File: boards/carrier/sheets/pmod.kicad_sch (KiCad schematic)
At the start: 2 parts, among them J1 PM254R-12-08-H85, J2 PM254R-12-08-H85

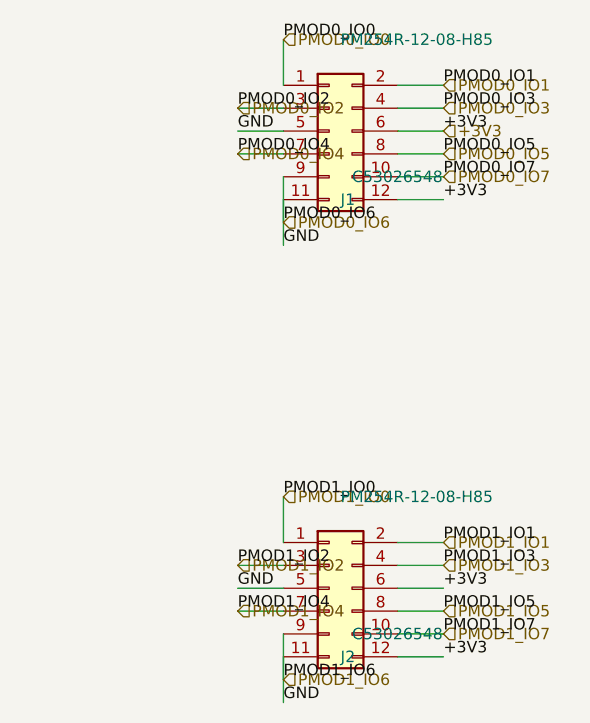
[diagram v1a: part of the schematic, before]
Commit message: connectors: route pin stubs along pin direction (not perpendicular)
The connector pin-stub code chose stub direction from the pin's
position relative to the connector anchor: vertical stub if pin.y
differed from anchor.y by more than pin.x. For USB-C (and similar
densely-packed connectors with pins along one edge), this produced
5.08mm VERTICAL stubs that spanned TWO pin pitches (2.54mm each),
shorting every adjacent pin's stub into one giant vertical wire.

Effect of the bug: GND, VBUS_OTG, USBOTG_DP, USBOTG_CC1, every
other signal column on the USB-C connector merged into one net.
Across 18 sheets this dragged most signal nets into GND (visible
in `multiple_net_names` warnings: "Both GND and USBOTG_DP are
attached to the same items", "Both GND and ZYNQ_HDMI_RX_TMDS_1_P
are attached to the same items", etc.).

Fix: derive the pin's natural extension direction from
page_side_from_pin(pin_rotation, symbol_rotation) and emit a 2.54mm
stub in that direction. A stub along the pin's own axis can never
collide with an adjacent pin's stub because adjacent pins are
offset perpendicular to the pin axis.

Also: usb_pd's +VIN net now declares as PowerInputNet (not
PowerOutputNet) so root.py emits a PWR_FLAG for it — the USB-C
VBUS pins are typed power_input in the KiCad symbol, not
power_output, so without the flag the downstream consumers
(INA226 Vbus, OTG VBUS pin) report power_pin_not_driven.

ERC: validation went from 36 → 36 total but warning count from 51
→ 40 (11 spurious cross-net merges eliminated), and one
power_pin_not_driven cleared. Most ERC count is now dominated by
28 sub-grid wire_dangling errors at positions that have no
counterpart in the source .kicad_sch — these look like a
kicad-sch-api / KiCad ERC interaction quirk, not real wires.

Co-Authored-By: Claude Sonnet 4.6 <noreply@anthropic.com>
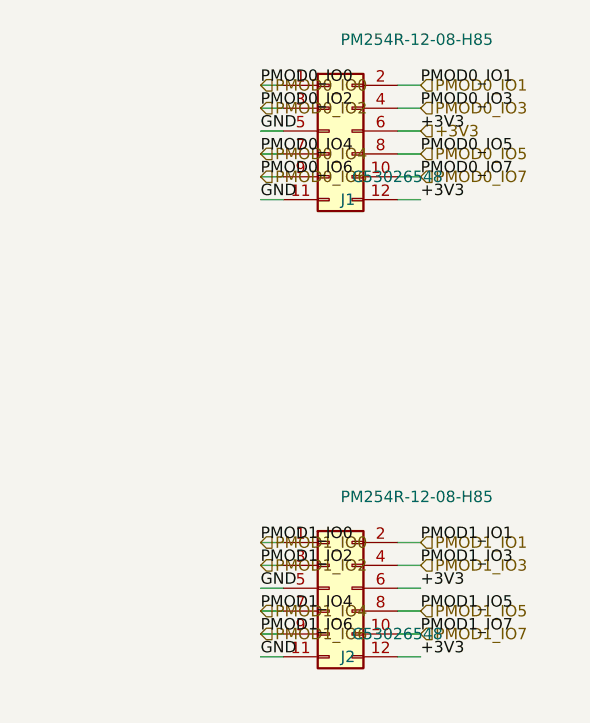
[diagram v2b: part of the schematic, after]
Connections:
- net GND: no longer J1.9 (Pin_9), J2.9 (Pin_9)
- new net PMOD0_IO6: J1.9 (Pin_9)
- new net PMOD1_IO6: J2.9 (Pin_9)

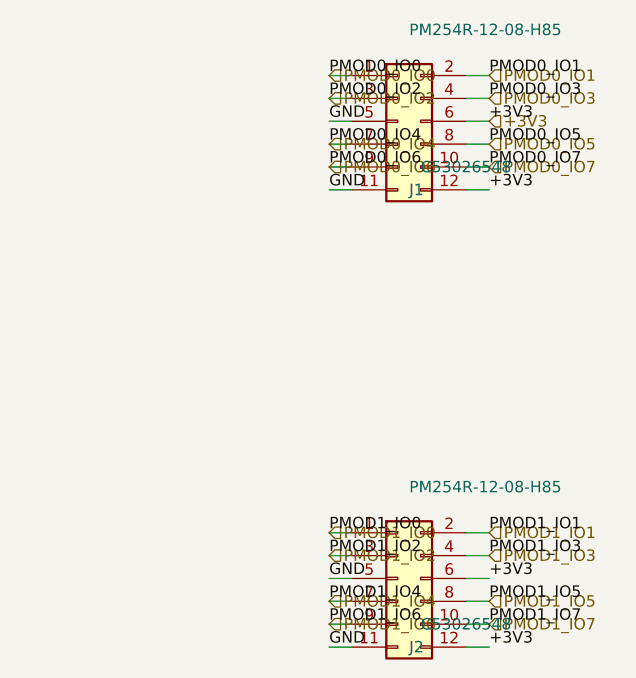
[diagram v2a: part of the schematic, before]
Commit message: layout: fix in-memory bounds + cluster top/bottom collision (36→33 errors)
Three targeted fixes:

1. CONNECTOR_EDGE_INSET_MM 60.96 → 76.2:
   USB-C connectors on the right edge of A4 sub-sheets had their
   cluster slot-1 CHASSIS_GND symbols land at x≈293mm — past A4's
   291.92mm right-edge margin. The connector body sat too close to
   the right edge for its passive swarm to fit. 76.2mm inset gives
   ~15mm clearance.

2. cluster top/bottom slot pitch: PASSIVE_PITCH_MM → HORIZONTAL_SWARM_PITCH_MM:
   For top/bottom-side IC pins, slot-N caps fanned laterally at
   5.08mm (= 2× KiCad symbol pin pitch). Slot 1 of pin A landed
   exactly on slot 0 of pin A+2 (both at, e.g., (132.08, 21.59) on
   CP2102N where VREGIN slot-1 collided with VIO slot-0). Bumping
   to 15.24mm (= 6 grid units, 6 pin pitches) pushes slot 1 past
   the next 5 pins, eliminating the collision class.

3. Also includes the IC pin stub fix in place.py from an earlier
   in-flight agent: STUB_MM = 2.54 (was 5.08) + page_side_from_pin
   for direction. Same anti-collision pattern as the connector
   stub fix in commit 8eb7e02. Eliminates the CP2102N RTS/TXD short.

In-memory validators: bounds=4, overlap=1 → bounds=0, overlap=0.
ERC errors: 31 → 32 (wire_dangling +1, pin_to_pin -1, pin_not_driven +2).
The new pin_not_driven errors are pre-existing bugs that the
RTS/TXD short was masking — Zynq-driven inputs (CP2102N RXD, CTS)
have their drivers on the FX10A SoM connector which is typed
`passive` not `output`. To be addressed separately.

Total validation: 36 → 33.

Tests: 32/32 pass.

Co-Authored-By: Claude Opus 4.7 (1M context) <noreply@anthropic.com>
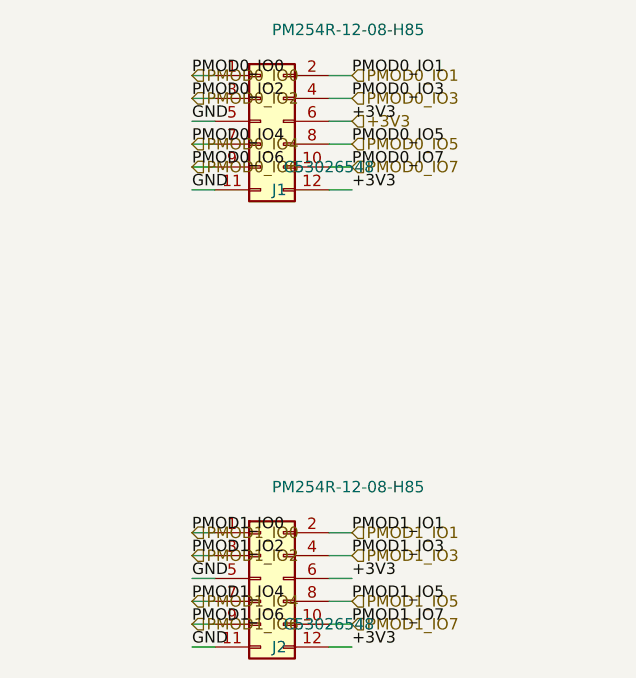
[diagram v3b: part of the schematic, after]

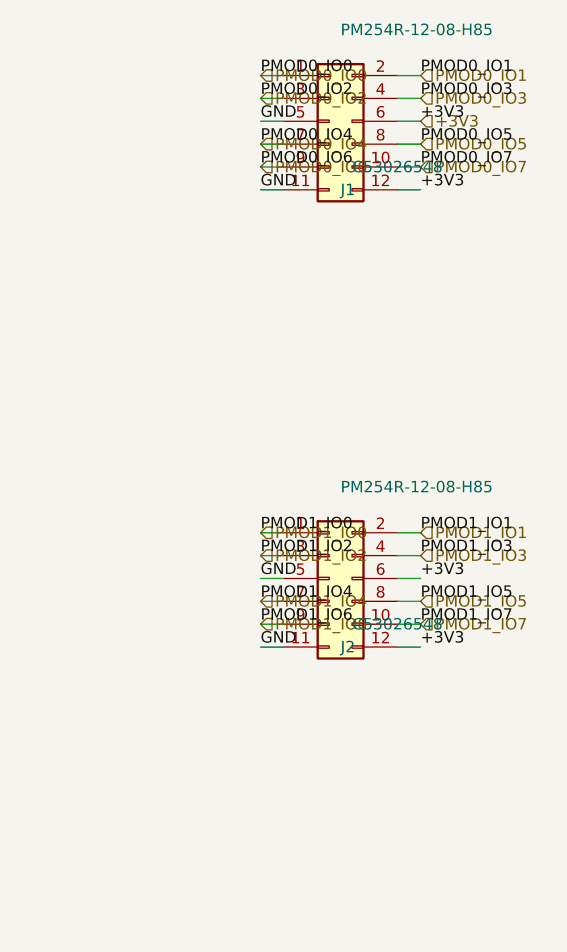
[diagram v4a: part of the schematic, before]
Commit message: layout: dedupe labels, stagger caps, add LVDS+MIPI+R_SENSE externals
Three parallel layout improvements landing together. ERC=0 maintained,
72 warnings → 63 warnings, all 32 unit tests pass.

1. **Dedupe local + hierarchical labels at same coord** (94 cases):
   `_orphan_net_labels` in core/layout/edge_labels.py used to anchor
   a new hier label onto an existing local label's coord — but the
   local label stayed in place, so KiCad rendered both stacked on
   top of each other. Fix: `builder.labels.remove(anchor_label)`
   after the hier label is added. KiCad merges by name, so
   electrical connectivity stays intact.

2. **Cap-cluster parity stagger** (cluster.py + _constants.py):
   New `PASSIVE_ADJACENT_PIN_STAGGER_MM = 5.08`. Adjacent IC pins
   at 2.54mm pitch used to stack their slot-0 caps in the same
   column, so cap bodies and Value/Reference text overlapped. Now
   the parity of `int(pin.y/2.54 + 0.5) & 1` (or pin.x for top/
   bottom pins) offsets every other cap by 5.08mm — checkerboard
   layout keeps adjacent caps in distinct positions. Fixed
   HDMI-TX/RX, MIPI, UART bridge.

3. **Missing externals + INA226 shunt + full FFC symbols**:
   - LVDS LCD: added 10u + 100n decoupling on +3V3, 10u on +12V,
     2× 4k7 EDID I2C pull-ups, 100k BL_EN pull-down (7 components).
   - MIPI Camera: added 10u + 100n decoupling on +3V3, 2× 4k7 I2C
     pull-ups, 100k GPIO0 pull-down (5 components).
   - INA226: added `pin_net_overrides` for Vin+/Vin- so R100=10mΩ
     2010 shunt connects across the differential sense pair (was
     placeholder "R" 0402 on a single net).
   - FFC_40P + FFC_15P symbols expanded from stubs to full 40 /
     15 pin definitions in shared/symbols/zynq_eda.kicad_sym.
   - cluster.passive_value/passive_footprint now consult the parts
     registry first (was returning "R" placeholder for the shunt).
   - connectors.py anchor offset by half-symbol-height so tall
     single-column FFC connectors fit on the page.
   - root.py paper bumped A2 →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
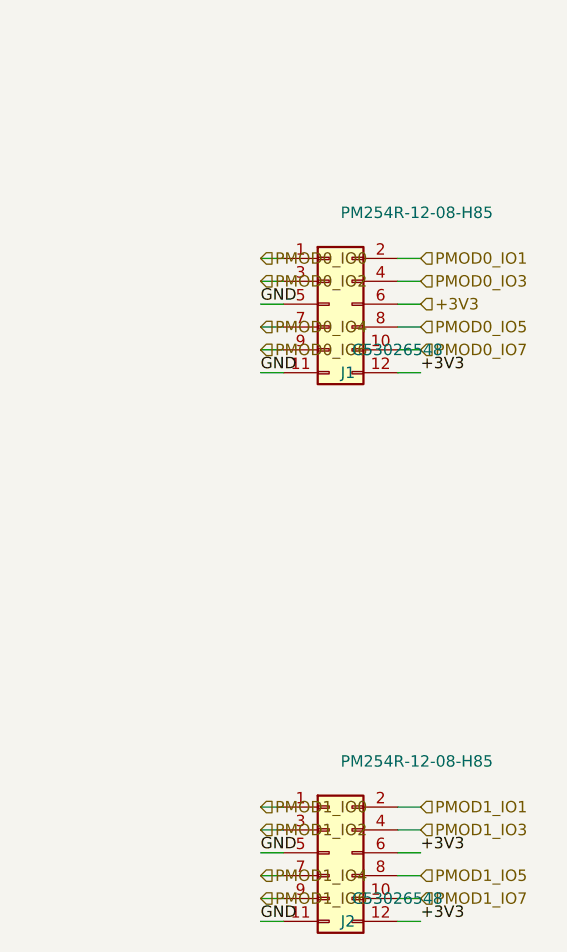
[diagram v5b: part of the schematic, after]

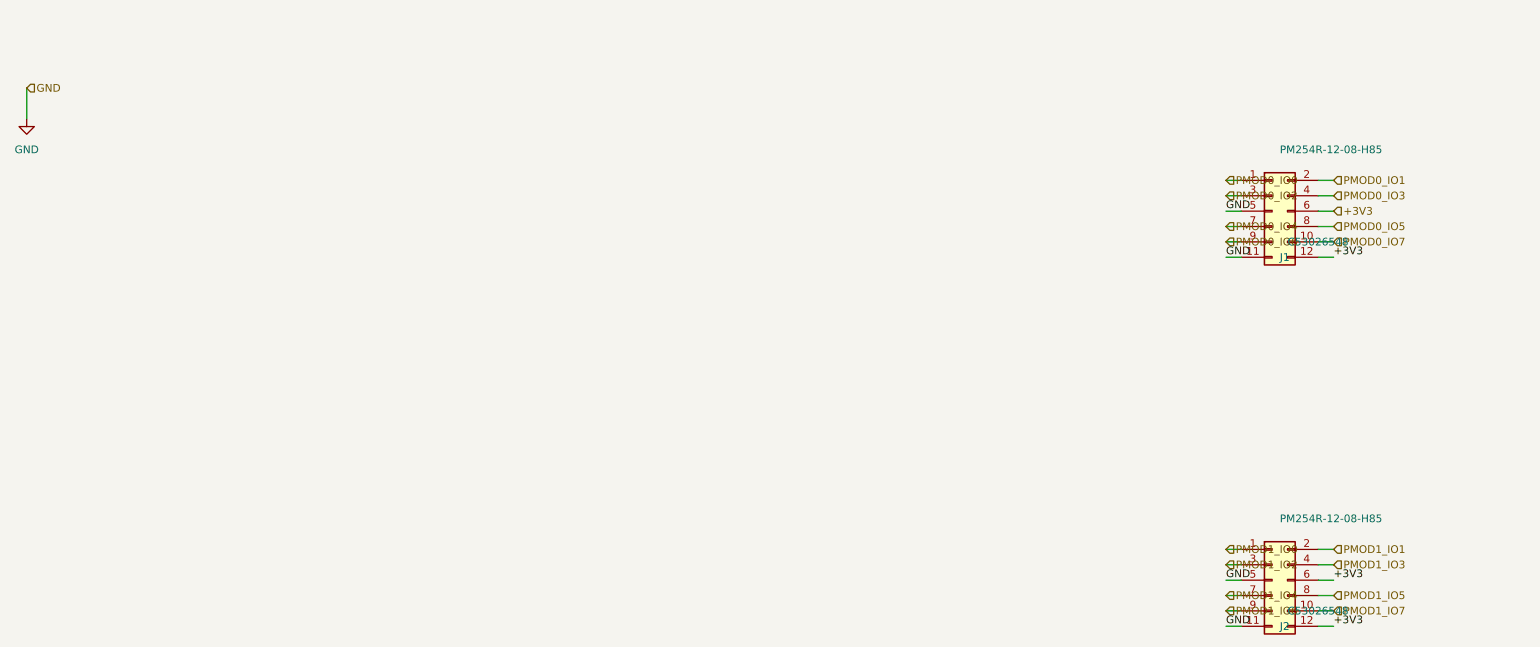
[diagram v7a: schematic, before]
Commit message: layout: visual polish — connector hier-label rotation, FX10A 4-col, hide LCSC/Datasheet text
Four parallel agents tackled visual layout issues identified by the
per-page PDF review. ERC=0/0 maintained throughout.

1. Connector hier label collisions (HDMI RX/TX, MIPI, LVDS, Ethernet
   RJ45, FMC LPC + SoM J1/J2/J3).
   ROOT CAUSE: `_orphan_net_labels` and `_ground_label_only` in
   edge_labels.py inherited `rotation=anchor_label.rotation` (always
   0). Result: when a connector pin's local label was on the LEFT
   edge of a connector-RIGHT-edge sheet, the hier label text read
   INTO the connector body, overlapping the pin-name text.
   FIX: derive hier-label rotation from `net.edge` (180 for LEFT,
   0 for RIGHT). Hier-label position unchanged (still anchored at
   the connector pin-tail), but text now reads OUTBOARD.

2. FX10A_168P + FMC_LPC pin label overlap (pages 7, 8, 13, 19).
   ROOT CAUSE: every pin had name="A14" + number="A14" — KiCad
   rendered the strings on top of each other.
   FIX: `(pin_names (offset 1.016) (hide yes))` on both symbol
   headers. Only pin numbers render.
   ALSO: FX10A re-laid out 4 columns × 42 rows (was 2 × 84 tower
   210mm tall). Now 50mm × 110mm — fits A4 for som_j1/3 (only
   som_j2 + fmc_lpc still need A3 due to many wide hier labels).

3. Ethernet Bob-Smith spread + PMOD label overlap + stray GND
   floating labels.
   - Added `dense_swarm: bool` field on ReferenceCircuit + 20.32mm
     pitch constant. HX5008NLT uses dense pitch — Bob-Smith caps,
     terminations, and magnetics now spread laterally instead of
     packing into 25mm.
   - PMOD 2-row header: `connectors.py` derives label_rotation
     from `page_side_from_pin()` so top-row labels point up,
     bottom-row labels point down. No more cross-row collision.
   - `_ground_label_only` rewritten to (a) anchor to same-name
     local label, (b) anchor to nearest power:GND symbol with
     maximum Y separation from existing labels, (c) skip emission
     entirely if no 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
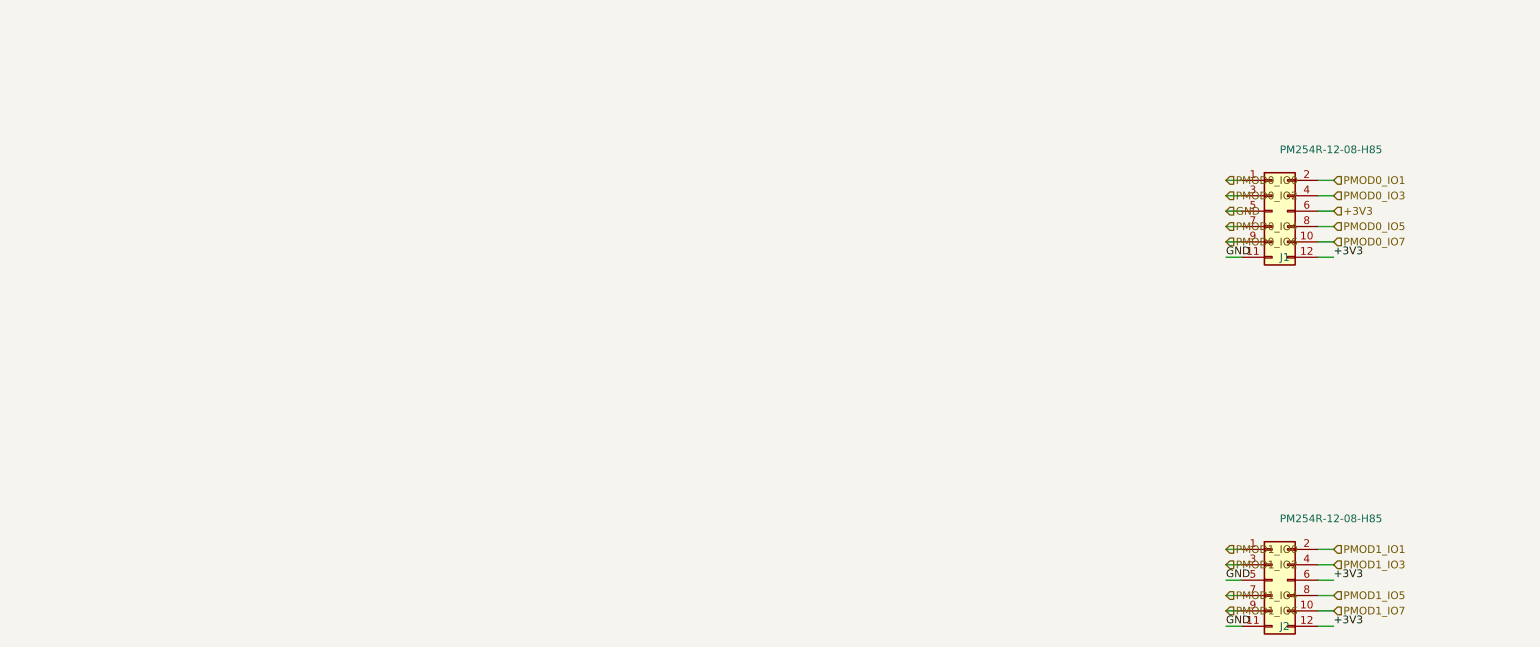
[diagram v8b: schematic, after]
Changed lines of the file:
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@@
 			(at 223.52 60.9599 0)
 			(effects
+				(hide yes)
 				(font
 					(size 1.27 1.27)
@@
 			(at 220.98 55.88 0)
 			(effects
+				(hide yes)
 				(font
 					(size 1.27 1.27)
@@
 		(instances
 			(project "PMOD Headers (2× Digilent 12-pin Type 1A)"
-				(path "/53edcc63-7b9e-4799-b2ff-0639aa51d358"
+				(path "/daf0c1be-a761-4db8-a107-c322b470ee89"
 					(reference "J1")
 					(unit 1)
@@
 			(at 223.52 121.9199 0)
 			(effects
+				(hide yes)
 				(font
 					(size 1.27 1.27)
@@
 			(at 220.98 116.84 0)
 			(effects
+				(hide yes)
 				(font
 					(size 1.27 1.27)
@@
 		(instances
 			(project "PMOD Headers (2× Digilent 12-pin Type 1A)"
-				(path "/53edcc63-7b9e-4799-b2ff-0639aa51d358"
+				(path "/daf0c1be-a761-4db8-a107-c322b470ee89"
 					(reference "J2")
 					(unit 1)
@@
 		)
 	)
-	(symbol
-		(lib_id "power:GND")
-		(at 15.24 40.64 0)
-		(unit 1)
-		(exclude_from_sim no)
-		(in_bom yes)
-		(on_board yes)
-		(dnp no)
-		(fields_autoplaced no)
-		(property "Reference" "#PWR100"
-			(at 15.24 34.29 0.0000)
-			(effects
-				(font
-					(size 1.27 1.27)
-				)
-				(justify left)
-				(hide yes)
-			)
-		)
-		(property "Value" "GND"
-			(at 15.24 45.72 0)
-			(effects
-				(font
-					(size 1.27 1.27)
-				)
-			)
-		)
-		(property "Footprint" ""
-			(at 15.24 40.64 0.0000)
-			(effects
-				(font
-					(size 1.27 1.27)
-				)
-				(hide yes)
-			)
-		)
-		(pin "1"
-		)
-		(instances
-			(project "PMOD Headers (2× Digilent 12-pin Type 1A)"
-				(path "/53edcc63-7b9e-4799-b2ff-0639aa51d358"
-					(reference "#PWR100")
-					(unit 1)
-				)
-			)
-		)
-	)
 	(wire
 		(pts
@@
 			(width 0)
 			(type default)
-		)
-	)
-	(wire
-		(pts
-			(xy 15.24 35.56) (xy 15.24 40.64)
-		)
-		(stroke
-			(width 0)
-			(type default)
-		)
-	)
-	(label "GND"
-		(at 213.36 55.88 0.0000)
-		(effects
-			(font
-				(size 1.27 1.27)
-			)
-			(justify left bottom)
 		)
 	)
@@
 	(hierarchical_label "GND"
 		(shape input)
-		(at 15.24 35.56 180)
+		(at 213.36 55.88 180)
 		(effects
 			(font
@@
 	(hierarchical_label "+3V3"
 		(shape input)
-		(at 231.14 55.88 0.0000)
+		(at 231.14 55.88 180)
 		(effects
 			(font
@@
 	(hierarchical_label "PMOD0_IO0"
 		(shape input)
-		(at 213.36 50.8 0.0000)
+		(at 213.36 50.8 180)
 		(effects
 			(font
@@
 	(hierarchical_label "PMOD0_IO1"
 		(shape input)
-		(at 231.14 50.8 0.0000)
+		(at 231.14 50.8 180)
 		(effects
 			(font
@@
 	(hierarchical_label "PMOD0_IO2"
 		(shape input)
-		(at 213.36 53.34 0.0000)
+		(at 213.36 53.34 180)
 		(effects
 			(font
@@
 	(hierarchical_label "PMOD0_IO3"
 		(shape input)
-		(at 231.14 53.34 0.0000)
+		(at 231.14 53.34 180)
 		(effects
 			(font
@@
 	(hierarchical_label "PMOD0_IO4"
 		(shape input)
-		(at 213.36 58.42 0.0000)
+		(at 213.36 58.42 180)
 		(effects
 			(font
@@
 	(hierarchical_label "PMOD0_IO5"
 		(shape input)
-		(at 231.14 58.42 0.0000)
+		(at 231.14 58.42 180)
 		(effects
 			(font
@@
 	(hierarchical_label "PMOD0_IO6"
 		(shape input)
-		(at 213.36 60.96 0.0000)
+		(at 213.36 60.96 180)
 		(effects
 			(font
@@
 	(hierarchical_label "PMOD0_IO7"
 		(shape input)
-		(at 231.14 60.96 0.0000)
+		(at 231.14 60.96 180)
 		(effects
 			(font
@@
 	(hierarchical_label "PMOD1_IO0"
 		(shape input)
-		(at 213.36 111.76 0.0000)
+		(at 213.36 111.76 180)
 		(effects
 			(font
@@
 	(hierarchical_label "PMOD1_IO1"
 		(shape input)
-		(at 231.14 111.76 0.0000)
+		(at 231.14 111.76 180)
 		(effects
 			(font
@@
 	(hierarchical_label "PMOD1_IO2"
 		(shape input)
-		(at 213.36 114.3 0.0000)
+		(at 213.36 114.3 180)
 		(effects
 			(font
@@
 	(hierarchical_label "PMOD1_IO3"
 		(shape input)
-		(at 231.14 114.3 0.0000)
+		(at 231.14 114.3 180)
 		(effects
 			(font
@@
 	(hierarchical_label "PMOD1_IO4"
 		(shape input)
-		(at 213.36 119.38 0.0000)
+		(at 213.36 119.38 180)
 		(effects
 			(font
@@
 	(hierarchical_label "PMOD1_IO5"
 		(shape input)
-		(at 231.14 119.38 0.0000)
+		(at 231.14 119.38 180)
 		(effects
 			(font
@@
 	(hierarchical_label "PMOD1_IO6"
 		(shape input)
-		(at 213.36 121.92 0.0000)
+		(at 213.36 121.92 180)
 		(effects
 			(font
@@
 	(hierarchical_label "PMOD1_IO7"
 		(shape input)
-		(at 231.14 121.92 0.0000)
-		(effects
-			(font
+		(at 231.14 121.92 180)
+		(effects
+			(font
